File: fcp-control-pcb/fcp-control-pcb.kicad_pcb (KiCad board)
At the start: 2 copper layers, 144.8 x 128.3 mm, 218 parts, among them IC1 L01Z050S05, J1 Conn_01x15_Female, J10 LittlePump, J11 BigPump, J12 OUT0, J13 Conn_01x10_Male, J14 Conn_01x10_Male, J15 Conn_01x10_Male, J2 Conn_01x15_Female, J3 CAPACITOR, J4 FUELCELL, J6 DISCHARGER, J7 CHARGER, J8 LimiterBypass, J9 Current_Mode, Q1 AONR21321, Q2 Q_NMOS_GDS, Q3 Q_NMOS_GDS, Q4 Q_NMOS_GDS, U1 MAX15462AB, U10 LM2902, U11 LM2902, U12 LM2902, U13 CD74HC4067SM, U14 CD74HC4067SM, U2 LM311DR, U3 TLI4971-A050T5-U-E0001, U5 LM2902, U6 LM2902, U7 LM2902, U8 LM2902, U9 LM2902

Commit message: queen r1.1
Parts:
- removed C17, C18, C19, C20, C21, C22: 0.1 uF, Capacitor_SMD:C_0805_2012Metric_Pad1.18x1.45mm_HandSolder
- removed D1, D2: D, custom:TSOT-23-3(2)
- removed R10, R106, R107, R108, R109, R11, R110, R111, R112, R113, R114, R115, R116, R117, R12, R13, R14, R15, R16, R17, R18, R19, R20, R21, R22, R23, R24, R25, R42, R43, R44, R45, R46, R47, R48, R49, R50, R51, R52, R53, R54, R55, R56, R57, R74, R75, R76, R77, R78, R79, R80, R81, R82, R83, R84, R85, R86, R87, R88, R89: 20k, Resistor_SMD:R_0402_1005Metric_Pad0.72x0.64mm_HandSolder
- removed R100, R101, R102, R103, R104, R105, R118, R119, R120, R121, R122, R123, R124, R125, R126, R127, R128, R129, R26, R27, R28, R29, R30, R31, R32, R33, R34, R35, R36, R37, R38, R39, R40, R41, R58, R59, R60, R61, R62, R63, R64, R65, R66, R67, R68, R69, R70, R71, R72, R73, R90, R91, R92, R93, R94, R95, R96, R97, R98, R99: 91k, Resistor_SMD:R_0402_1005Metric_Pad0.72x0.64mm_HandSolder
- removed U11, U12: LM2902, Package_SO:SOIC-14_3.9x8.7mm_P1.27mm
- removed U13, U14: CD74HC4067SM, Package_SO:SSOP-24_5.3x8.2mm_P0.65mm
- added J16: ExtraAnalogs, Connector_PinHeader_2.54mm:PinHeader_1x02_P2.54mm_Vertical, F.Cu at (242.2, 57.0)
- added J5: ArduinoVCCPower, Connector_PinHeader_2.54mm:PinHeader_1x02_P2.54mm_Vertical, F.Cu at (221.4, 73.5)
- added RN1: 3.3k, Package_SO:SOIC-16_4.55x10.3mm_P1.27mm, F.Cu at (82.5, 52.1)
- added RN2: 3.3k, Package_SO:SOIC-16_4.55x10.3mm_P1.27mm, F.Cu at (82.5, 81.3)
- added RN3: 3.3k, Package_SO:SOIC-16_4.55x10.3mm_P1.27mm, F.Cu at (71.1, 104.1)
- added RN4: 3.3k, Package_SO:SOIC-16_4.55x10.3mm_P1.27mm, F.Cu at (69.8, 34.3)
- added RN5: 1k, Package_SO:SOIC-16_4.55x10.3mm_P1.27mm, F.Cu at (83.8, 67.3)
- added RN6: 1k, Package_SO:SOIC-16_4.55x10.3mm_P1.27mm, F.Cu at (82.5, 94.0)
- added RN7: 1k, Package_SO:SOIC-16_4.55x10.3mm_P1.27mm, F.Cu at (76.2, 116.8)
- added RN8: 1k, Package_SO:SOIC-16_4.55x10.3mm_P1.27mm, F.Cu at (87.6, 34.3)
- added U4: AS78L05RTR-G1, Package_TO_SOT_SMD:SOT-89-3_Handsoldering, F.Cu at (215.0, 74.2)
- C13, C15: value 0.1 uF -> 0.33uF; moved to F.Cu
- C14, C16: value 0.1 uF -> 0.1uF
- C5: value 1uF -> 10uF
- R2: moved to F.Cu
- U1: footprint digikey-footprints:TDFN-8-1EP -> Package_DFN_QFN:TDFN-8-1EP_2x2mm_P0.5mm_EP0.8x1.2mm
- U10, U8: value LM2902 -> ADC1283; footprint Package_SO:SOIC-14_3.9x8.7mm_P1.27mm -> Package_SO:TSSOP-16_4.4x5mm_P0.65mm
- U5: value LM2902 -> ZXGD3003E6; footprint Package_SO:SOIC-14_3.9x8.7mm_P1.27mm -> Package_TO_SOT_SMD:SOT-23-6; moved to F.Cu
- U6: value LM2902 -> AS78L05RTR-G1; footprint Package_SO:SOIC-14_3.9x8.7mm_P1.27mm -> Package_TO_SOT_SMD:SOT-89-3_Handsoldering
- U7, U9: value LM2902 -> ADC1283; footprint Package_SO:SOIC-14_3.9x8.7mm_P1.27mm -> Package_SO:TSSOP-16_4.4x5mm_P0.65mm; moved to F.Cu
- moved U5 209.2 mm to (273.2, 38.5)
- moved U6 197.5 mm to (252.7, 51.2)
- moved C16 168.3 mm to (261.6, 37.8), turned to 0 degrees
- moved U10 163.8 mm to (244.3, 51.4), turned to 0 degrees
- moved C15 162.6 mm to (251.1, 55.7)
- moved U9 145.3 mm to (226.1, 40.6), turned to 0 degrees
- moved C14 134.7 mm to (218.2, 79.9)
- moved C13 133.2 mm to (213.4, 78.7)
- moved R2 115.0 mm to (273.1, 42.2), turned to 0 degrees
- moved U8 56.6 mm to (91.4, 57.1), turned to -90 degrees
- moved U7 46.2 mm to (76.2, 45.7), turned to 180 degrees
- moved J13 40.6 mm to (57.8, 75.7)
- moved J14 23.3 mm to (69.2, 56.7)
- moved J15 1.27 mm to (57.8, 36.3)
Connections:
- A1 pad 12: /BigPump -> /LittlePump
- A1 pad 6: /D3 -> /ADCSelect0
- A1 pad 7: /D4 -> /ADCSelect1
- A1 pad 8: /D5 -> /ADCSelect2
- A1 pad 9: /D6 -> /ADCSelect3
- C13 pad 1: /Voltage Sensing/VCC -> VCC
- C14 pad 1: /Voltage Sensing/VCC -> +5VA
- C15 pad 1: /Voltage Sensing/VCC -> VCC
- C16 pad 1: +5V -> +5VA
- J1 pad 12: /BigPump -> /LittlePump
- J1 pad 6: /D3 -> /ADCSelect0
- J1 pad 7: /D4 -> /ADCSelect1
- J1 pad 8: /D5 -> /ADCSelect2
- J1 pad 9: /D6 -> /ADCSelect3
- Q1 pad 4: Net-(J8-Pad2) -> Net-(Q1-Pad4)
- Q2 pad 1: /D10 -> /LittlePump
- Q3 pad 1: /BigPump -> /D8
- Q4 pad 1: /D8 -> /D7
- R7 pad 2: /D10 -> /LittlePump
- R8 pad 2: /BigPump -> /D8
- R9 pad 2: /D8 -> /D7
- U10 pad 1: /Voltage Sensing/Cell 20 -> /ADCSelect0
- U10 pad 10: Net-(R86-Pad1) -> /Voltage Sensing/cell7
- U10 pad 11: GND -> /Voltage Sensing/cell8
- U10 pad 12: Net-(R88-Pad1) -> unconnected-(U10-Pad12)
- U10 pad 13: Net-(R105-Pad2) -> +5V
- U10 pad 14: /Voltage Sensing/Cell 17 -> /MOSI
- U10 pad 2: Net-(R102-Pad2) -> +5VA
- U10 pad 3: Net-(R82-Pad1) -> GND
- U10 pad 4: /Voltage Sensing/VCC -> /Voltage Sensing/cell1
- U10 pad 5: Net-(R84-Pad1) -> /Voltage Sensing/cell2
- U10 pad 6: Net-(R103-Pad2) -> /Voltage Sensing/cell3
- U10 pad 7: /Voltage Sensing/Cell 19 -> /Voltage Sensing/cell4
- U10 pad 8: /Voltage Sensing/Cell 18 -> /Voltage Sensing/cell5
- U10 pad 9: Net-(R104-Pad2) -> /Voltage Sensing/cell6
- U5 pad 1: /Voltage Sensing/Cell 8 -> /Current Sensing/FC_OUT
- U5 pad 2: Net-(R11-Pad1) -> Net-(J8-Pad2)
- U5 pad 3: Net-(R10-Pad1) -> GND
- U5 pad 4: /Voltage Sensing/VCC -> Net-(Q1-Pad4)
- U5 pad 5: Net-(R12-Pad1) -> Net-(J8-Pad2)
- U5 pad 6: Net-(R13-Pad1) -> Net-(Q1-Pad4)
- U6 pad 1: /Voltage Sensing/Cell 4 -> +5VA
- U6 pad 2: Net-(R19-Pad1) -> GND
- U6 pad 3: Net-(R18-Pad1) -> VCC
- U7 pad 1: /Voltage Sensing/Cell 16 -> /ADCSelect3
- U7 pad 10: Net-(R46-Pad1) -> /Voltage Sensing/extra1
- U7 pad 11: GND -> /Voltage Sensing/extra2
- U7 pad 12: Net-(R48-Pad1) -> GND
- U7 pad 13: Net-(R49-Pad1) -> +5V
- U7 pad 14: /Voltage Sensing/Cell 13 -> /MISO
- U7 pad 2: Net-(R43-Pad1) -> +5VA
- U7 pad 3: Net-(R42-Pad1) -> GND
- U7 pad 4: /Voltage Sensing/VCC -> /Voltage Sensing/cell25
- U7 pad 5: Net-(R44-Pad1) -> /Voltage Sensing/cell26
- U7 pad 6: Net-(R45-Pad1) -> /Voltage Sensing/cell27
- U7 pad 7: /Voltage Sensing/Cell 15 -> /Voltage Sensing/cell28
- U7 pad 8: /Voltage Sensing/Cell 14 -> /Voltage Sensing/cell29
- U7 pad 9: Net-(R47-Pad1) -> /Voltage Sensing/cell30
- U8 pad 1: /Voltage Sensing/Cell 12 -> /ADCSelect2
- U8 pad 10: Net-(R54-Pad1) -> /Voltage Sensing/cell23
- U8 pad 11: GND -> /Voltage Sensing/cell24
- U8 pad 12: Net-(R56-Pad1) -> GND
- U8 pad 13: Net-(R57-Pad1) -> +5V
- U8 pad 14: /Voltage Sensing/Cell 9 -> /MISO
- U8 pad 2: Net-(R51-Pad1) -> +5VA
- U8 pad 3: Net-(R50-Pad1) -> GND
- U8 pad 4: /Voltage Sensing/VCC -> /Voltage Sensing/cell17
- U8 pad 5: Net-(R52-Pad1) -> /Voltage Sensing/cell18
- U8 pad 6: Net-(R53-Pad1) -> /Voltage Sensing/cell19
- U8 pad 7: /Voltage Sensing/Cell 11 -> /Voltage Sensing/cell20
- U8 pad 8: /Voltage Sensing/Cell 10 -> /Voltage Sensing/cell21
- U8 pad 9: Net-(R55-Pad1) -> /Voltage Sensing/cell22
- U9 pad 1: /Voltage Sensing/Cell 24 -> /ADCSelect1
- U9 pad 10: Net-(R78-Pad1) -> /Voltage Sensing/cell15
- U9 pad 11: GND -> /Voltage Sensing/cell16
- U9 pad 12: Net-(R80-Pad1) -> GND
- U9 pad 13: Net-(R101-Pad2) -> +5V
- U9 pad 14: /Voltage Sensing/Cell 21 -> /MISO
- U9 pad 2: Net-(R75-Pad1) -> +5VA
- U9 pad 3: Net-(R74-Pad1) -> GND
- U9 pad 4: /Voltage Sensing/VCC -> /Voltage Sensing/cell9
- U9 pad 5: Net-(R76-Pad1) -> /Voltage Sensing/cell10
- U9 pad 6: Net-(R77-Pad1) -> /Voltage Sensing/cell11
- U9 pad 7: /Voltage Sensing/Cell 23 -> /Voltage Sensing/cell12
- U9 pad 8: /Voltage Sensing/Cell 22 -> /Voltage Sensing/cell13
- U9 pad 9: Net-(R100-Pad2) -> /Voltage Sensing/cell14
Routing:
- net GND: track 206.4 -> 35.2 mm, vias 45 -> 4
- net /Voltage Sensing/VCC: track 90.4 -> 0.00 mm, vias 9 -> 0
- net /D6: track 85.5 -> 0.00 mm
- net /D4: track 85.2 -> 0.00 mm, vias 2 -> 0
- net /D5: track 73.7 -> 0.00 mm, vias 3 -> 0
- net /Analog1: track 76.5 -> 5.08 mm, vias 2 -> 0
- net /D10: track 75.2 -> 4.41 mm
- net /Voltage Sensing/Cell 3: track 69.6 -> 0.00 mm, vias 2 -> 0
- net /BigPump: track 68.5 -> 0.00 mm
- net /LittlePump: track 0.00 -> 67.9 mm
- net /Analog0: track 71.6 -> 5.08 mm, vias 2 -> 0
- net /MOSI: track 57.3 -> 4.41 mm, vias 3 -> 0
- net /Voltage Sensing/Cell 16: track 49.8 -> 0.00 mm, vias 3 -> 0
- net Net-(R50-Pad1): track 49.3 -> 0.00 mm, vias 4 -> 0
- net /Voltage Sensing/Cell 15: track 49.1 -> 0.00 mm, vias 1 -> 0
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- added copper zone on B.Cu, net (none)
- added copper zone on B.Cu, net /Current Sensing/FC_OUT
- removed copper zone on B.Cu, net /Voltage Sensing/VCC
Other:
- board text added: "+"
- board text added: "-"
- board text added: "Queen"
- board text added: "Safety"
- board text added: "Telemetry"
- board text removed: "FCP Control 2.0"

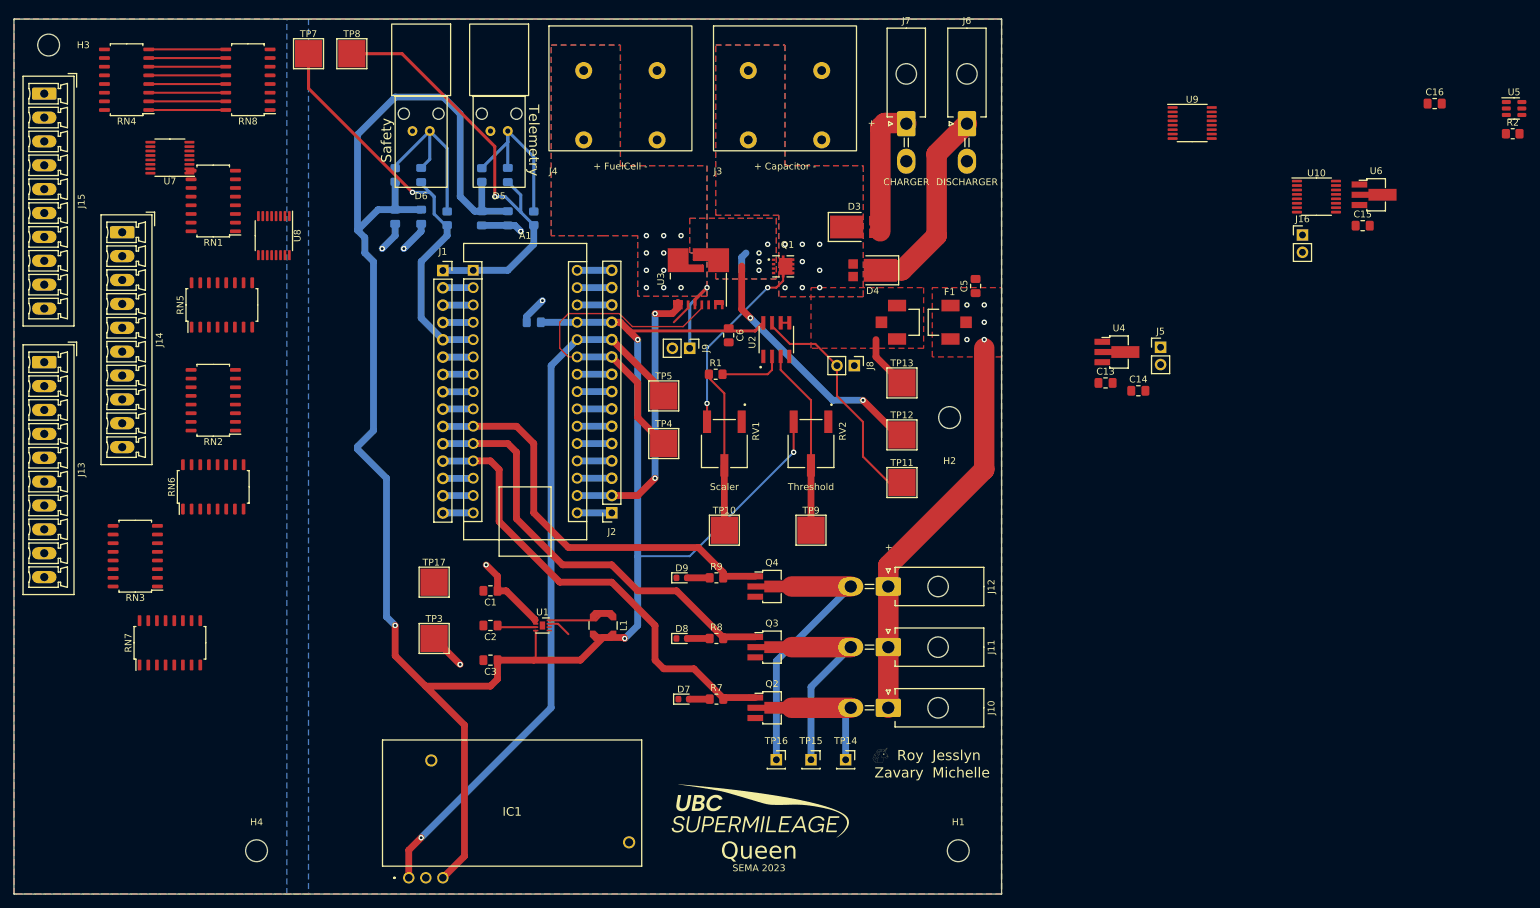
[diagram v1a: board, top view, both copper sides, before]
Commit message: resize board
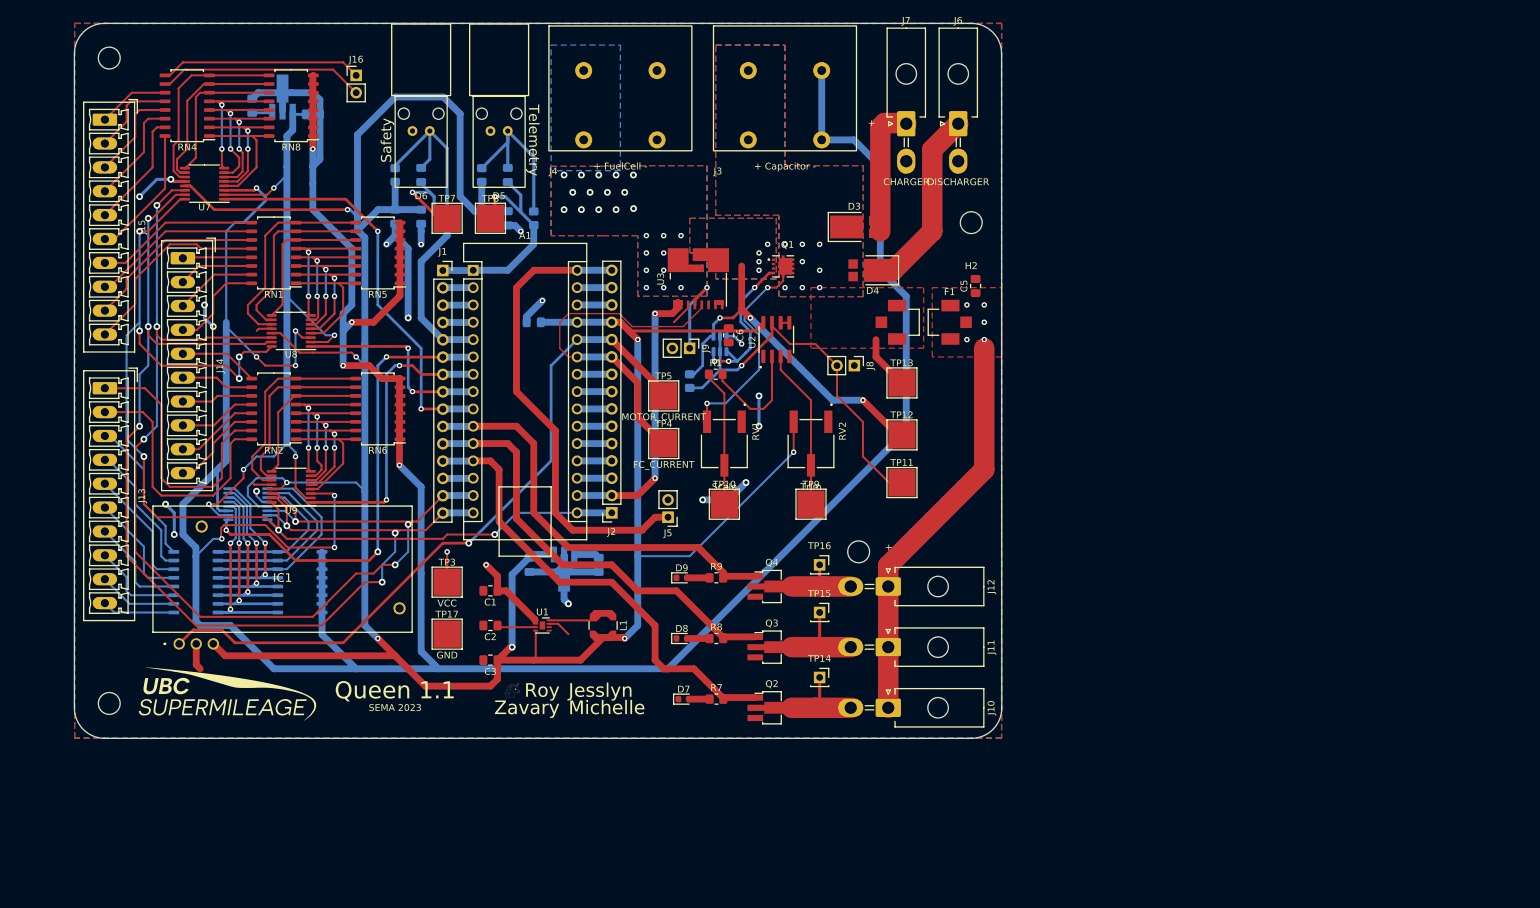
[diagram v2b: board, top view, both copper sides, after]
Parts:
- C13, C14, C15, C16, R2, RN3, RN7, U10, U4, U5, U6: moved to B.Cu
- moved C16 164.5 mm to (97.2, 39.4)
- moved C15 163.7 mm to (88.3, 38.1), turned to 90 degrees
- moved U10 163.0 mm to (87.6, 96.5)
- moved U6 160.7 mm to (92.7, 36.8), turned to 90 degrees
- moved U9 142.4 mm to (94.0, 94.0), turned to 180 degrees
- moved J16 140.7 mm to (103.5, 33.7)
- moved R2 126.0 mm to (152.4, 78.5), turned to -90 degrees
- moved U5 121.4 mm to (156.8, 73.0), turned to -90 degrees
- moved C14 92.8 mm to (128.9, 105.4), turned to -90 degrees
- moved U4 87.1 mm to (134.0, 106.0), turned to -90 degrees
- moved G*** 80.0 mm to (84.5, 125.1)
- moved C13 78.9 mm to (139.1, 105.4), turned to -90 degrees
- moved J5 76.4 mm to (149.2, 98.4), turned to 180 degrees
- moved G*** 54.8 mm to (126.4, 123.8)
- moved IC1 48.0 mm to (77.6, 117.0)
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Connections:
- C14 pad 1: +5VA -> +5V
- RN3 pad 1: /Voltage Sensing/cell1 -> Net-(J13-Pad10)
- RN3 pad 10: Net-(J13-Pad4) -> /Voltage Sensing/cell7
- RN3 pad 11: Net-(J13-Pad5) -> /Voltage Sensing/cell6
- RN3 pad 12: Net-(J13-Pad6) -> /Voltage Sensing/cell5
- RN3 pad 13: Net-(J13-Pad7) -> /Voltage Sensing/cell4
- RN3 pad 14: Net-(J13-Pad8) -> /Voltage Sensing/cell3
- RN3 pad 15: Net-(J13-Pad9) -> /Voltage Sensing/cell2
- RN3 pad 16: Net-(J13-Pad10) -> /Voltage Sensing/cell1
- RN3 pad 2: /Voltage Sensing/cell2 -> Net-(J13-Pad9)
- RN3 pad 3: /Voltage Sensing/cell3 -> Net-(J13-Pad8)
- RN3 pad 4: /Voltage Sensing/cell4 -> Net-(J13-Pad7)
- RN3 pad 5: /Voltage Sensing/cell5 -> Net-(J13-Pad6)
- RN3 pad 6: /Voltage Sensing/cell6 -> Net-(J13-Pad5)
- RN3 pad 7: /Voltage Sensing/cell7 -> Net-(J13-Pad4)
- RN3 pad 8: /Voltage Sensing/cell8 -> Net-(J13-Pad3)
- RN3 pad 9: Net-(J13-Pad3) -> /Voltage Sensing/cell8
- RN5 pad 1: unconnected-(RN5-Pad1) -> GND
- RN5 pad 2: unconnected-(RN5-Pad2) -> GND
- RN5 pad 3: unconnected-(RN5-Pad3) -> GND
- RN5 pad 4: unconnected-(RN5-Pad4) -> GND
- RN5 pad 5: unconnected-(RN5-Pad5) -> GND
- RN5 pad 6: unconnected-(RN5-Pad6) -> GND
- RN5 pad 7: unconnected-(RN5-Pad7) -> GND
- RN5 pad 8: unconnected-(RN5-Pad8) -> GND
- RN6 pad 1: unconnected-(RN6-Pad1) -> GND
- RN6 pad 2: unconnected-(RN6-Pad2) -> GND
- RN6 pad 3: unconnected-(RN6-Pad3) -> GND
- RN6 pad 4: unconnected-(RN6-Pad4) -> GND
- RN6 pad 5: unconnected-(RN6-Pad5) -> GND
- RN6 pad 6: unconnected-(RN6-Pad6) -> GND
- RN6 pad 7: unconnected-(RN6-Pad7) -> GND
- RN6 pad 8: unconnected-(RN6-Pad8) -> GND
- RN7 pad 1: unconnected-(RN7-Pad1) -> /Voltage Sensing/cell1
- RN7 pad 10: /Voltage Sensing/cell7 -> GND
- RN7 pad 11: /Voltage Sensing/cell6 -> GND
- RN7 pad 12: /Voltage Sensing/cell5 -> GND
- RN7 pad 13: /Voltage Sensing/cell4 -> GND
- RN7 pad 14: /Voltage Sensing/cell3 -> GND
- RN7 pad 15: /Voltage Sensing/cell2 -> GND
- RN7 pad 16: /Voltage Sensing/cell1 -> GND
- RN7 pad 2: unconnected-(RN7-Pad2) -> /Voltage Sensing/cell2
- RN7 pad 3: unconnected-(RN7-Pad3) -> /Voltage Sensing/cell3
- RN7 pad 4: unconnected-(RN7-Pad4) -> /Voltage Sensing/cell4
- RN7 pad 5: unconnected-(RN7-Pad5) -> /Voltage Sensing/cell5
- RN7 pad 6: unconnected-(RN7-Pad6) -> /Voltage Sensing/cell6
- RN7 pad 7: unconnected-(RN7-Pad7) -> /Voltage Sensing/cell7
- RN7 pad 8: unconnected-(RN7-Pad8) -> /Voltage Sensing/cell8
- RN7 pad 9: /Voltage Sensing/cell8 -> GND
- RN8 pad 1: unconnected-(RN8-Pad1) -> GND
- RN8 pad 2: unconnected-(RN8-Pad2) -> GND
- RN8 pad 3: unconnected-(RN8-Pad3) -> GND
- RN8 pad 4: unconnected-(RN8-Pad4) -> GND
- RN8 pad 5: unconnected-(RN8-Pad5) -> GND
- RN8 pad 6: unconnected-(RN8-Pad6) -> GND
- RN8 pad 7: unconnected-(RN8-Pad7) -> GND
- RN8 pad 8: unconnected-(RN8-Pad8) -> GND
- U10 pad 12: unconnected-(U10-Pad12) -> GND
- U4 pad 1: +5VA -> +5V
- U7 pad 14: /MISO -> /MOSI
- U8 pad 14: /MISO -> /MOSI
- U9 pad 14: /MISO -> /MOSI
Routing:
- net GND: track 35.2 -> 594.2 mm, vias 4 -> 29
- net /MISO: track 4.46 -> 168.3 mm, vias 0 -> 6
- net /MOSI: track 4.41 -> 168.0 mm, vias 0 -> 6
- net /SCK: track 5.08 -> 158.0 mm, vias 0 -> 7
- net +5VA: track 0.00 -> 105.3 mm, vias 0 -> 5
- net +5V: track 327.6 -> 410.9 mm, vias 4 -> 8
- net /VinNano: track 5.08 -> 68.8 mm
- net /ADCSelect0: track 4.41 -> 68.1 mm, vias 0 -> 3
- net /ADCSelect3: track 4.41 -> 60.8 mm, vias 0 -> 2
- net Net-(J13-Pad1): track 0.00 -> 40.2 mm
- net /ADCSelect1: track 4.41 -> 43.4 mm, vias 0 -> 2
- net Net-(J13-Pad2): track 0.00 -> 38.6 mm
- net /Voltage Sensing/cell24: track 0.00 -> 30.7 mm
- net /TLMTR_TX: track 64.3 -> 33.8 mm
- net Net-(J16-Pad2): track 0.00 -> 30.3 mm
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- removed copper zone on B.Cu, net (none)
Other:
- board size 144.8 x 128.3 mm -> 136 x 104.8 mm
- board text added: "Queen 1.1"
- board text added: "Scale"
- board text added: "Trim"
- board text removed: "Queen"
- board text removed: "Scaler"
- board text removed: "Threshold"

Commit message: label tps
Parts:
- moved TP11 0.64 mm to (183.5, 94.0)
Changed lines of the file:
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@@
   )
   (footprint "TestPoint:TestPoint_Pad_4.0x4.0mm" (layer "F.Cu")
-    (at 183.515 93.345)
+    (at 183.515 93.98)
     (descr "SMD rectangular pad as test Point, square 4.0mm side length")
     (tags "test point SMD pad rectangle square")
@@
       (effects (font (size 1 1) (thickness 0.15)))
     )
-    (fp_text value "COMP+" (at 0 3.1) (layer "F.Fab")
+    (fp_text value "COMP+" (at 0 3.1) (layer "F.SilkS")
       (effects (font (size 1 1) (thickness 0.15)))
     )
@@
       (effects (font (size 1 1) (thickness 0.15)))
     )
-    (fp_text value "V_FC" (at 0 3.1) (layer "F.Fab")
+    (fp_text value "V_FC" (at 0 3.1) (layer "F.SilkS")
       (effects (font (size 1 1) (thickness 0.15)))
     )
@@
       (effects (font (size 1 1) (thickness 0.15)))
     )
-    (fp_text value "COMP-" (at 0 3.1) (layer "F.Fab")
+    (fp_text value "COMP-" (at 0 3.1) (layer "F.SilkS")
       (effects (font (size 1 1) (thickness 0.15)))
     )
@@
       (effects (font (size 1 1) (thickness 0.15)))
     )
-    (fp_text value "V_CAP" (at 0 3.1) (layer "F.Fab")
+    (fp_text value "V_CAP" (at 0 3.1) (layer "F.SilkS")
       (effects (font (size 1 1) (thickness 0.15)))
     )

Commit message: Queen 1.1
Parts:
- added J17: AnalogPower, Connector_Molex:Molex_Mini-Fit_Jr_5569-02A2_2x01_P4.20mm_Horizontal, F.Cu at (102.9, 40.2)
- TP4: value FC_CURRENT -> I_FC
- TP5: value MOTOR_CURRENT -> I_MOTOR
- moved J16 27.7 mm to (76.2, 29.2), turned to 90 degrees
- moved H1 4.44 mm to (177.2, 99.1)
- moved IC1 1.43 mm to (77.6, 118.4)
- moved TP10 1.27 mm to (157.5, 97.8)
- moved TP9 1.27 mm to (170.2, 97.8)
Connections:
- net /D8 renamed /BigPump
- net /LittlePump renamed /D9
- C15 pad 1: VCC -> +12VA
- C15 pad 2: GND -> GNDA
- C16 pad 2: GND -> GNDA
- RN5 pad 1: GND -> GNDA
- RN5 pad 2: GND -> GNDA
- RN5 pad 3: GND -> GNDA
- RN5 pad 4: GND -> GNDA
- RN5 pad 5: GND -> GNDA
- RN5 pad 6: GND -> GNDA
- RN5 pad 7: GND -> GNDA
- RN5 pad 8: GND -> GNDA
- RN6 pad 1: GND -> GNDA
- RN6 pad 2: GND -> GNDA
- RN6 pad 3: GND -> GNDA
- RN6 pad 4: GND -> GNDA
- RN6 pad 5: GND -> GNDA
- RN6 pad 6: GND -> GNDA
- RN6 pad 7: GND -> GNDA
- RN6 pad 8: GND -> GNDA
- RN7 pad 10: GND -> GNDA
- RN7 pad 11: GND -> GNDA
- RN7 pad 12: GND -> GNDA
- RN7 pad 13: GND -> GNDA
- RN7 pad 14: GND -> GNDA
- RN7 pad 15: GND -> GNDA
- RN7 pad 16: GND -> GNDA
- RN7 pad 9: GND -> GNDA
- RN8 pad 1: GND -> GNDA
- RN8 pad 2: GND -> GNDA
- RN8 pad 3: GND -> GNDA
- RN8 pad 4: GND -> GNDA
- RN8 pad 5: GND -> GNDA
- RN8 pad 6: GND -> GNDA
- RN8 pad 7: GND -> GNDA
- RN8 pad 8: GND -> GNDA
- U10 pad 3: GND -> GNDA
- U6 pad 2: GND -> GNDA
- U6 pad 3: VCC -> +12VA
- U7 pad 3: GND -> GNDA
- U8 pad 3: GND -> GNDA
- U9 pad 3: GND -> GNDA
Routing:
- net GND: track 594.2 -> 135.3 mm, vias 29 -> 20
- net GNDA: track 0.00 -> 283.6 mm, vias 0 -> 8
- net +12VA: track 0.00 -> 32.6 mm
- net Net-(J16-Pad2): track 30.3 -> 7.68 mm
- net Net-(J16-Pad1): track 29.6 -> 7.70 mm
- net +5V: track 410.9 -> 407.2 mm
- net VCC: track 81.6 -> 78.6 mm
- net /Analog7: track 102.4 -> 103.8 mm
- net Net-(J13-Pad10): track 11.8 -> 10.7 mm
- net Net-(J13-Pad3): track 22.4 -> 21.6 mm
- net /Voltage Sensing/cell30: track 22.8 -> 22.1 mm
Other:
- board text added: "1"
- board text added: "10"
- board text added: "11"
- board text added: "12"
- board text added: "13"
- board text added: "14"
- board text added: "15"
- board text added: "16"
- board text added: "17"
- board text added: "18"
- board text added: "19"
- board text added: "2"
- board text added: "20"
- board text added: "21"
- board text added: "22"
- board text added: "23"
- board text added: "24"
- board text added: "25"
- board text added: "26"
- board text added: "27"
- board text added: "28"
- board text added: "29"
- board text added: "3"
- board text added: "30"
- board text added: "4"
- board text added: "5"
- board text added: "6"
- board text added: "7"
- board text added: "8"
- board text added: "9"
- board text added: "Analog Power"
- board text added: "Big Pump"
- board text added: "Little Pump"
- board text added: "Safety / Misc"
